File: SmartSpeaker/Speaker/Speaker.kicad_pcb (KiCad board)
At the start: 2 copper layers, 94 x 85.1 mm, 46 parts, among them J1 Terminal_2, J2 Terminal_3, J3 54-00166, Q1 DMG2305UX-13, U1 LM384, U2 LM4040LP-3, U3 LM2675N-5, U4 LTC1655LCN8

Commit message: run through DRC, make fixes
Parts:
- moved REF** 5.84 mm to (119.4, 103.4)
- moved C4 5.41 mm to (112.1, 81.3)
- moved R1 5.18 mm to (126.5, 89.9)
- moved REF** 4.58 mm to (115.3, 95.8)
- moved J1 4.26 mm to (134.8, 88.4)
- moved A1 3.84 mm to (81.8, 95.5)
- moved JP3 3.45 mm to (61.2, 80.5)
- moved JP2 0.81 mm to (57.1, 82.3)
- moved U2 0.40 mm to (68.6, 81.6)
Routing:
- net VDD: track 62.7 -> 56.6 mm
- net Net-(A1-3V3_OUT): track 4.57 -> 10.0 mm
- net Net-(A1-ADC_VREF): track 18.0 -> 15.5 mm
- net Net-(C4-Pad1): track 7.83 -> 10.2 mm
- net Net-(A1-GP19): track 9.72 -> 7.64 mm
- net Net-(U4-VOUT): track 12.5 -> 14.3 mm
- net /SpeakerOut: track 7.87 -> 9.66 mm
- net /AudioOut: track 38.4 -> 37.3 mm
- net Net-(A1-GP17): track 7.62 -> 8.69 mm
- net Net-(A1-GP18): track 7.62 -> 8.69 mm
- net Net-(A1-VSYS): track 4.59 -> 5.60 mm
- net Net-(JP2-B): track 4.77 -> 3.97 mm, vias 1 -> 0
- net (no net): track 0.65 -> 0.00 mm
- net /Adafruit_1713_Microphone/OUTPUT: track 51.8 -> 52.3 mm
- net Net-(A1-VBUS): track 12.3 -> 11.8 mm, vias 1 -> 0

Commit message: add some final titles and logos
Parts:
- added REF**: Symbol_Danger_8x8mm_Copper, Symbol:Symbol_Danger_8x8mm_Copper, F.Cu at (67.3, 66.5)
- moved TP3 13.1 mm to (109.5, 49.3)
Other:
- board text added: "SALE System: Smart Speaker Rev A. Calum McConnell"

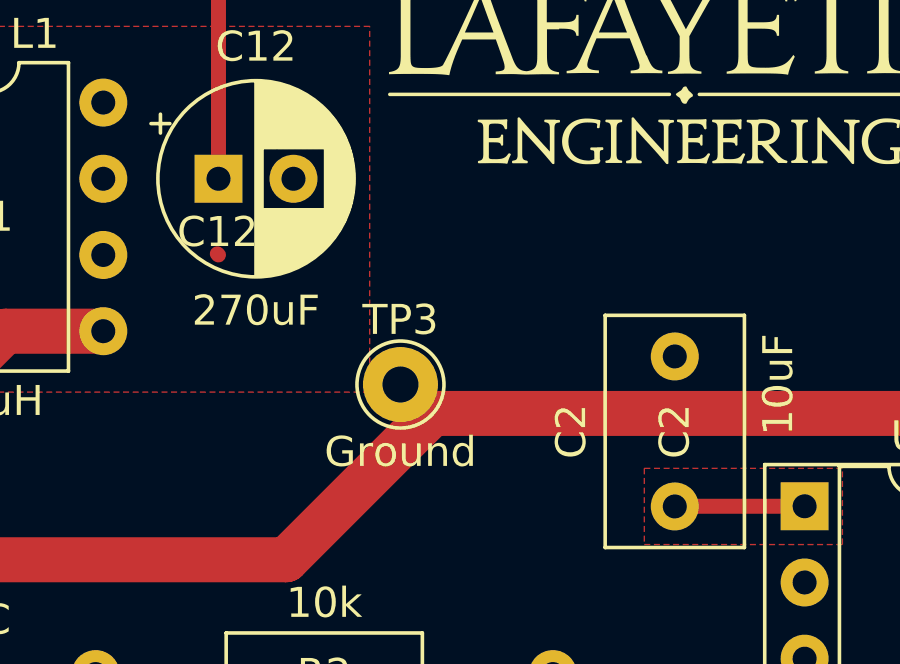
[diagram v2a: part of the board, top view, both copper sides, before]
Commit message: Fix ground short
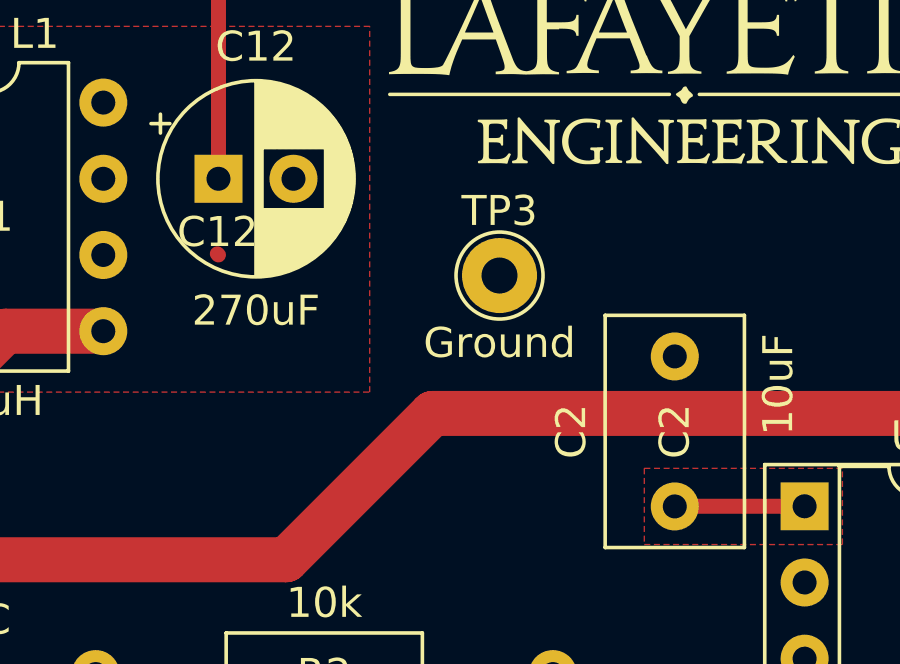
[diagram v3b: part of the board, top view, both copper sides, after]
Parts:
- moved TP3 4.91 mm to (112.8, 45.6)
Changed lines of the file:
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@@
 		(tags "test point THT pad")
 		(property "Reference" "TP3"
-			(at 0 -2.148 -0)
+			(at 0 -2.148 0)
 			(layer "B.SilkS")
 			(effects
@@
 		(tags "test point THT pad")
 		(property "Reference" "TP6"
-			(at 0 -2.148 -0)
+			(at 0 -2.148 0)
 			(layer "B.SilkS")
 			(effects
@@
 		(tags "test point THT pad")
 		(property "Reference" "TP5"
-			(at 0 -2.286 -0)
+			(at 0 -2.286 0)
 			(layer "B.SilkS")
 			(effects
@@
 		(tags "test point THT pad")
 		(property "Reference" "TP1"
-			(at 0 -2.148 -0)
+			(at 0 -2.148 0)
 			(layer "B.SilkS")
 			(effects
@@
 		(tags "CONN DEV")
 		(property "Reference" "JP1"
-			(at 1.3 -2 -0)
+			(at 1.3 -2 0)
 			(layer "B.SilkS")
 			(effects
@@
 		(tags "test point THT pad")
 		(property "Reference" "TP9"
-			(at 0 -2.148 -0)
+			(at 0 -2.148 0)
 			(layer "B.SilkS")
 			(effects
@@
 		(tags "test point THT pad")
 		(property "Reference" "TP8"
-			(at 0 -2.148 -0)
+			(at 0 -2.148 0)
 			(layer "B.SilkS")
 			(effects
@@
 		(tags "test point THT pad")
 		(property "Reference" "TP10"
-			(at 0 -2.148 -0)
+			(at 0 -2.148 0)
 			(layer "B.SilkS")
 			(effects
@@
 		(tags "test point THT pad")
 		(property "Reference" "TP3"
-			(at 0 -2.148 -0)
+			(at 0 -2.148 0)
 			(layer "B.SilkS")
 			(effects
@@
 		(tags "test point THT pad")
 		(property "Reference" "TP7"
-			(at 0 -2.148 -0)
+			(at 0 -2.148 0)
 			(layer "B.SilkS")
 			(effects
@@
 		(tags "test point THT pad")
 		(property "Reference" "TP4"
-			(at 0 -2.148 -0)
+			(at 0 -2.148 0)
 			(layer "B.SilkS")
 			(effects
@@
 		(tags "test point THT pad")
 		(property "Reference" "TP2"
-			(at 0 -2.148 -0)
+			(at 0 -2.148 0)
 			(layer "B.SilkS")
 			(effects
@@
 	(footprint "TestPoint:TestPoint_THTPad_D2.5mm_Drill1.2mm"
 		(layer "F.Cu")
-		(at 109.474 49.276)
+		(at 112.776 45.6438)
 		(descr "THT pad as test Point, diameter 2.5mm, hole diameter 1.2mm ")
 		(tags "test point THT pad")
 		(property "Reference" "TP3"
-			(at 0 -2.148 -0)
+			(at 0 -2.148 0)
 			(layer "B.SilkS")
 			(effects

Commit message: updates per wey
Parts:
- U2: footprint Package_TO_SOT_THT:TO-92_Inline -> Package_TO_SOT_THT:TO-92_Inline_Wide
- moved J2 20.1 mm to (68.1, 74.2)
- moved REF** 18.9 mm to (134.1, 98.0)
- moved REF** 17.7 mm to (53.2, 55.9)
- moved J1 13.3 mm to (122.2, 92.5)
- moved TP3 8.74 mm to (64.2, 52.8)
- moved R1 5.23 mm to (125.3, 84.8)
- moved TP10 2.72 mm to (76.6, 75.6)
- moved C4 2.62 mm to (110.1, 79.6)
- moved TP7 2.03 mm to (77.7, 82.0)
- moved TP5 1.83 mm to (120.1, 73.6)
- moved U2 1.13 mm to (67.5, 81.8)
- moved TP3 0.95 mm to (108.5, 74.1)
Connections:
- A1 pad 32: unconnected-(A1-GP27-Pad32) -> GND
- RV1 pad 1: Net-(C5-Pad1) -> GND
- RV1 pad 2: GND -> Net-(C5-Pad1)
- U2 pad 1: unconnected-(U2-NC-Pad1) -> GND
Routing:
- net /Adafruit_1713_Microphone/OUTPUT: track 52.3 -> 35.5 mm
- net /SpeakerOut: track 9.66 -> 15.6 mm
- net Net-(C4-Pad1): track 10.2 -> 5.24 mm
- net VDD: track 56.6 -> 61.1 mm
- net Net-(C5-Pad1): track 7.41 -> 11.2 mm
- net /AudioOut: track 37.3 -> 34.0 mm
- net /Power_converter/5VOut: track 112.9 -> 110.5 mm
- net Net-(A1-ADC_VREF): track 15.5 -> 13.5 mm

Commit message: improvements pre-manufacture
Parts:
- moved J1 2.18 mm to (121.7, 90.4)
- moved TP10 1.65 mm to (76.6, 73.9)
- moved TP8 1.15 mm to (95.0, 61.1)
- moved U2 1.09 mm to (67.5, 80.7)
- moved RV1 0.97 mm to (102.1, 67.1)
- moved TP7 0.61 mm to (77.7, 81.4)
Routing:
- net /Power_converter/VoltageIn: track 40.3 -> 46.0 mm
- net /Adafruit_1713_Microphone/OUTPUT: track 35.5 -> 33.8 mm
- net Net-(A1-ADC_VREF): track 13.5 -> 14.9 mm
- net Net-(U4-VOUT): track 14.2 -> 15.4 mm
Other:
- rule pad_to_mask_clearance: 0 -> 0.038
- board text added: "JLCJLCJLCJLC"

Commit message: final PCB updates, for realzies, probably
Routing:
- net Net-(A1-GP19): track 7.64 -> 18.4 mm
- net /Power_converter/VoltageIn: track 46.0 -> 47.3 mm
